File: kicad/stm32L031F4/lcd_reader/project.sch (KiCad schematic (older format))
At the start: 32 parts, among them J1 WAKE, J10 TEST_1P, J11 TEST_1P, J12 TEST_1P, J2 SWD, J3 TEST_1P, J4 TEST_1P, J5 TEST_1P, J6 LCD, J7 TEST_1P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

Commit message: Labels
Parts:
- added J13: GND_EXT, Pin_Headers:Pin_Header_Straight_1x01_Pitch2.54mm, symbol CONN_01X01
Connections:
- net GND: now also J13.1 (P1)
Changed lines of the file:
@@
 Wire Wire Line
 	3375 4900 3975 4900
+$Comp
+L CONN_01X01 J13
+U 1 1 5A01BD9F
+P 9900 5500
+F 0 "J13" H 9900 5600 50  0000 C CNN
+F 1 "GND_EXT" V 10000 5500 50  0000 C CNN
+F 2 "Pin_Headers:Pin_Header_Straight_1x01_Pitch2.54mm" H 9900 5500 50  0001 C CNN
+F 3 "" H 9900 5500 50  0001 C CNN
+	1    9900 5500
+	1    0    0    -1
+$EndComp
 $EndSCHEMATC

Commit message: Silkscreen tidying
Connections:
- net COM1: now also J6.1 (P1); no longer J6.9 (P9)
- net at R10.2, U3.13: now also J6.9 (P9); no longer J6.1 (P1)
- net at R9.2, U3.11: now also J6.8 (P8); no longer J6.2 (P2)
- net at R8.2, U3.9: now also J6.7 (P7); no longer J6.3 (P3)
- net at R7.2, U3.5: now also J6.6 (P6); no longer J6.4 (P4)
- net at R5.2, U1.11: now also J6.4 (P4); no longer J6.6 (P6)
- net at R4.2, U1.9: now also J6.3 (P3); no longer J6.7 (P7)
- net at R3.2, U1.5: now also J6.2 (P2); no longer J6.8 (P8)
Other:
- moved on the sheet: C4, C5, J10, J11, J12, J3, J4, J5, J6, J7, J9, R10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

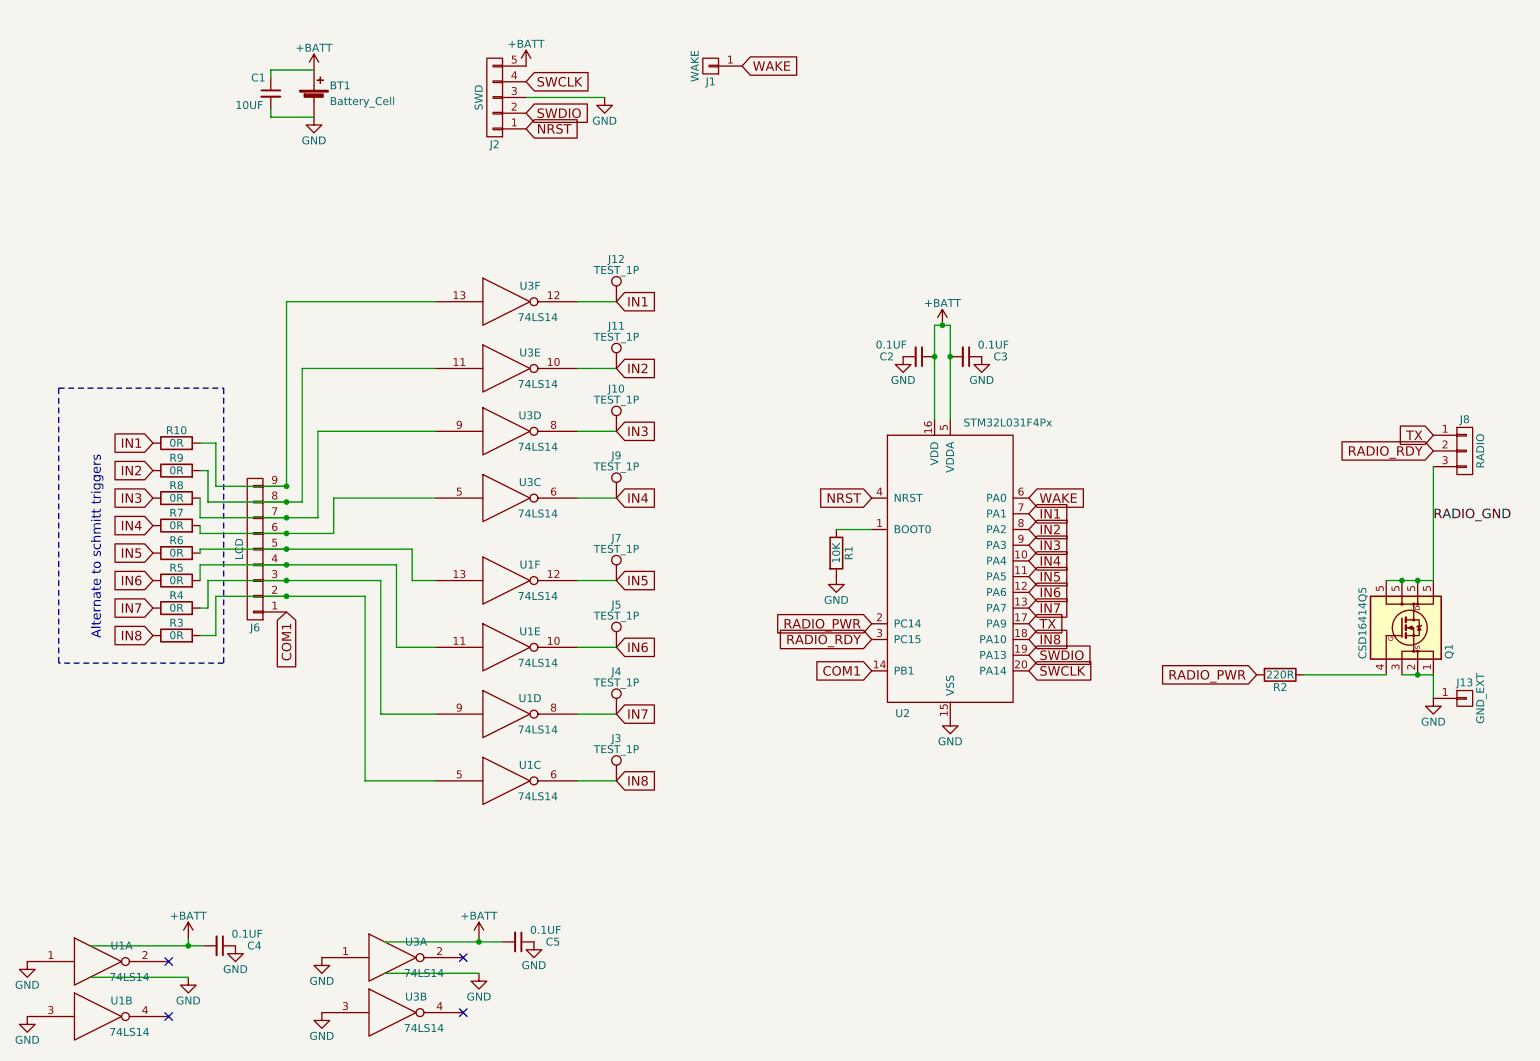
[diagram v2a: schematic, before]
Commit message: Start of zebra strip compatability
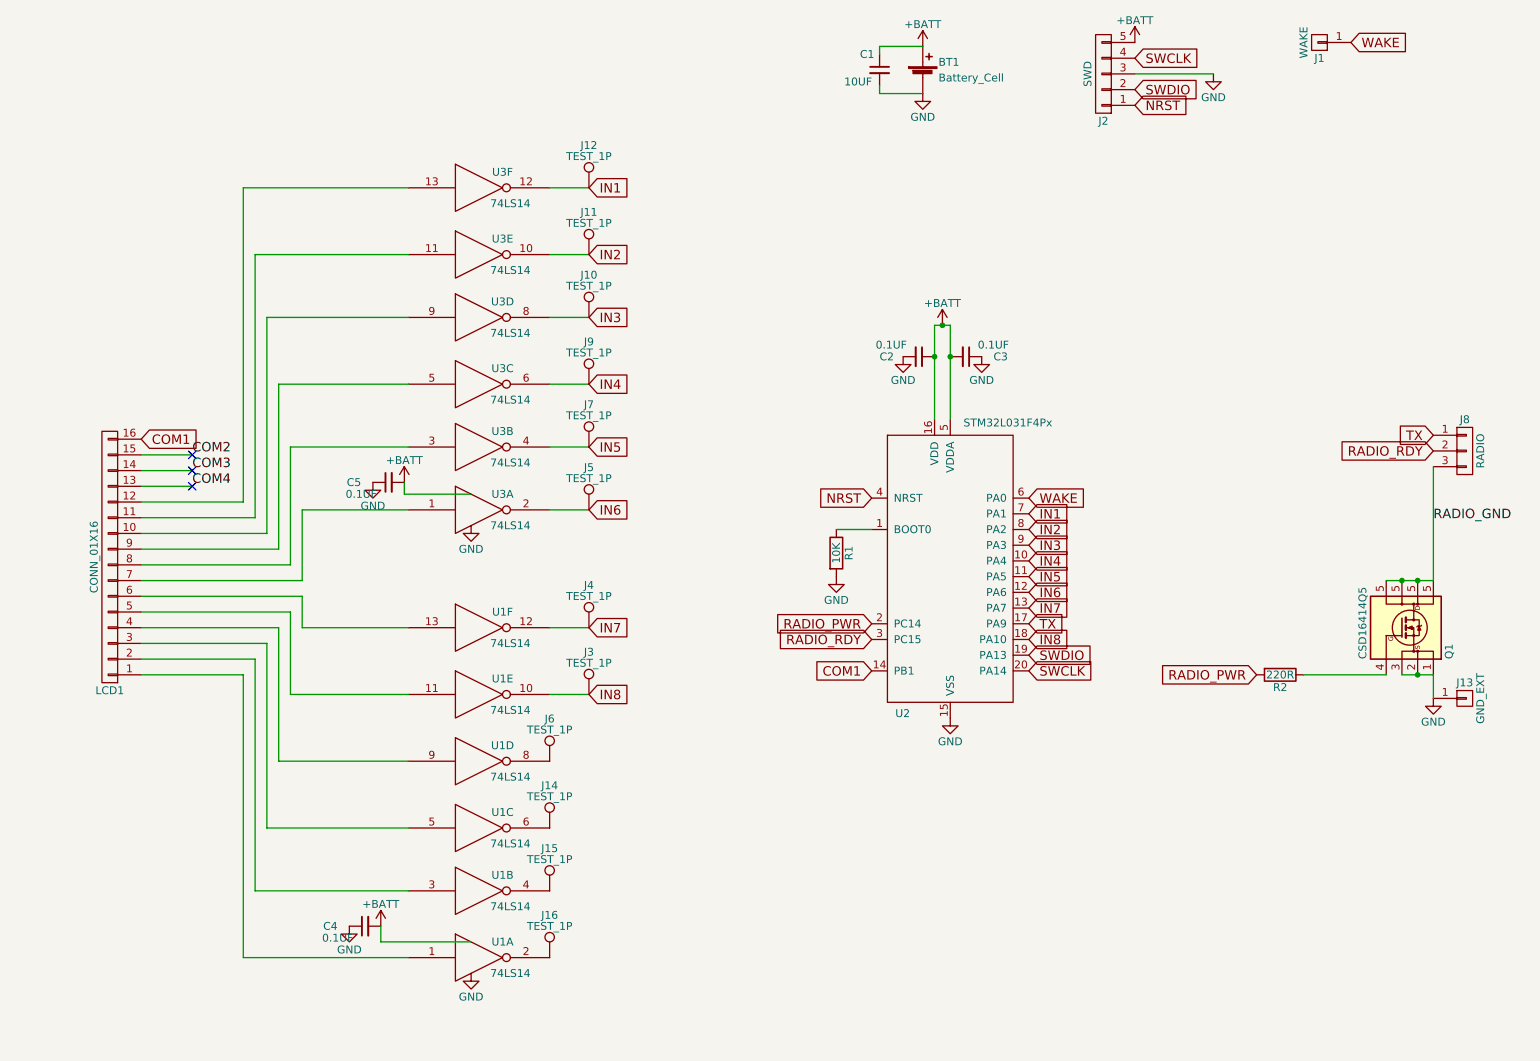
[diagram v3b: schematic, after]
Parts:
- removed J6: LCD, Pin_Headers:Pin_Header_Straight_1x09_Pitch2.54mm, symbol CONN_01X09
- removed R10, R3, R4, R5, R6, R7, R8, R9: 0R, Resistors_SMD:R_0603_HandSoldering, symbol R
- added J14, J15, J16, J6: TEST_1P, Connectors_TestPoints:Test_Point_Pad_d1.0mm, symbol TEST_1P
- added LCD1: CONN_01X16, theapi:ZEBRA-16, symbol CONN_01X16
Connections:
- net COM1: now also LCD1.16 (P16)
- net GND: no longer U1.1, U1.3, U3.1, U3.3
- net IN5: now also U3.4; no longer U1.12
- net IN6: now also U3.2; no longer U1.10
- net IN7: now also U1.12; no longer U1.8
- net IN8: now also U1.10; no longer U1.6
- net at U3.13: now also LCD1.12 (P12)
- net at U3.11: now also LCD1.11 (P11)
- net at U1.5: now also LCD1.3 (P3)
- net at U1.9: now also LCD1.4 (P4)
- net at U1.11: now also LCD1.5 (P5)
- net at U1.13: now also LCD1.6 (P6)
- net at U3.5: now also LCD1.9 (P9)
- net at U3.9: now also LCD1.10 (P10)
- net at U1.4: now also J15.1
- net at U1.2: now also J16.1
- new net: J6.1, U1.8
- new net: J14.1, U1.6
- new net: LCD1.8 (P8), U3.3
- new net: LCD1.7 (P7), U3.1
- new net: LCD1.2 (P2), U1.3
- new net: LCD1.1 (P1), U1.1
- new net COM2: LCD1.15 (P15)
- new net COM3: LCD1.14 (P14)
- new net COM4: LCD1.13 (P13)
- no-connect marks 4 -> 3
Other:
- note removed: "Alternate to schmitt triggers"
- moved on the sheet: BT1, C1, C4, C5, J1, J10, J11, J12, J2, J3, J4, J5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

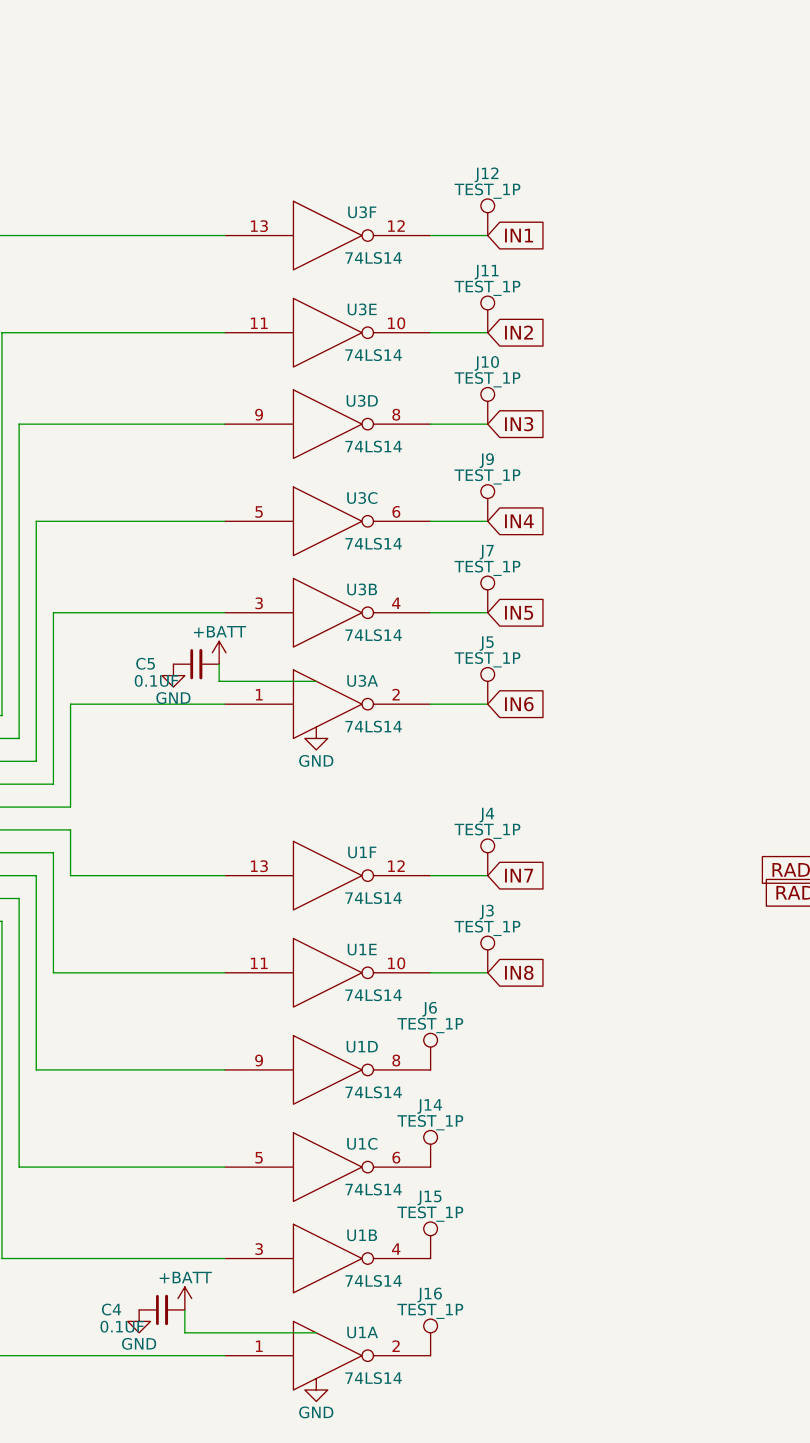
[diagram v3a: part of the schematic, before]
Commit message: Layout for sandwiched zebra connector
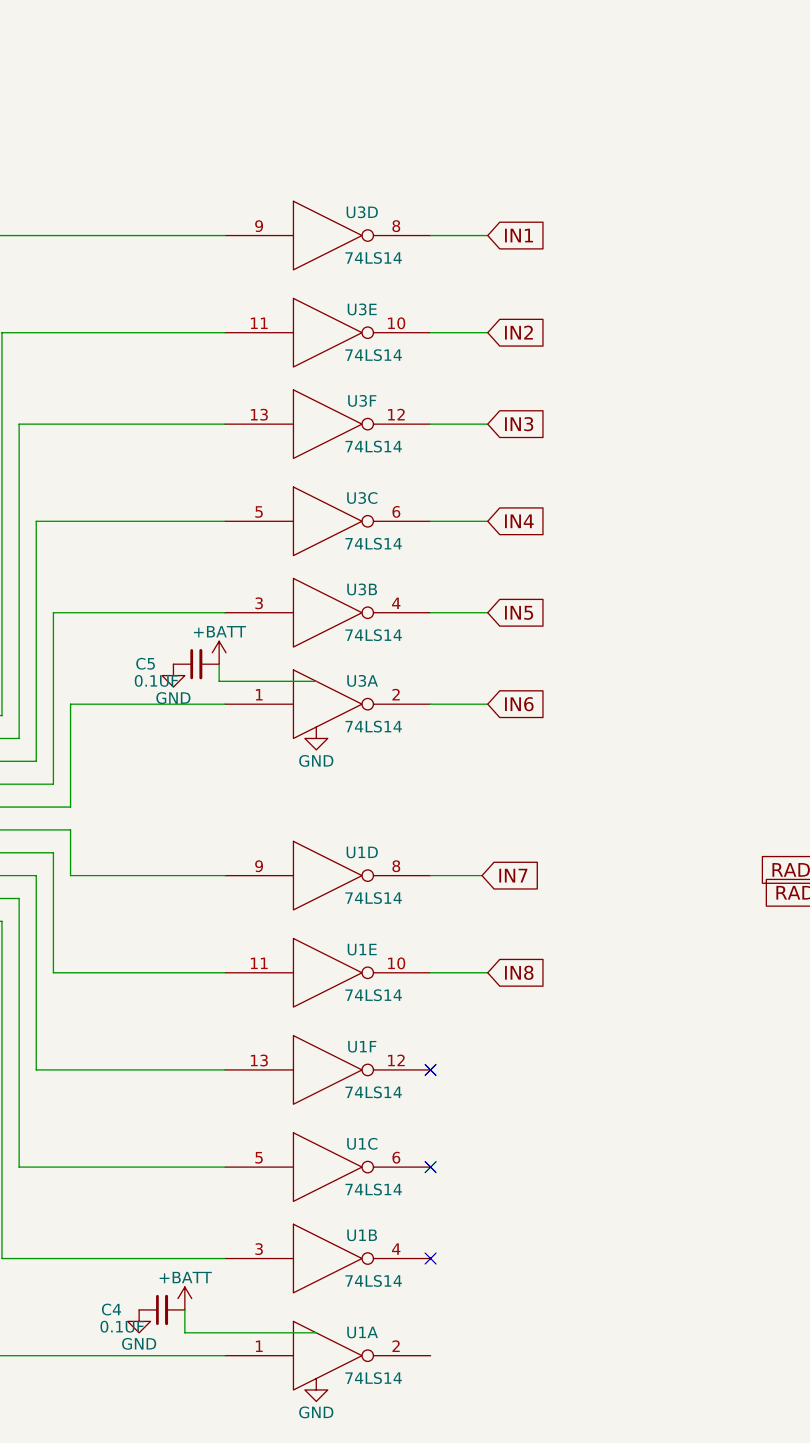
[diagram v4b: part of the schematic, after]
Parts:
- removed J10, J11, J12, J14, J15, J16, J3, J4, J5, J6, J7, J9: TEST_1P, Connectors_TestPoints:Test_Point_Pad_d1.0mm, symbol TEST_1P
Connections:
- net IN1: now also U3.8; no longer U3.12
- net IN3: now also U3.12; no longer U3.8
- net IN7: now also U1.8; no longer U1.12
- net at U3.13: now also LCD1.10 (P10); no longer LCD1.12 (P12)
- net at U3.9: now also LCD1.12 (P12); no longer LCD1.10 (P10)
- net at U1.13: now also LCD1.4 (P4); no longer LCD1.6 (P6)
- net at U1.9: now also LCD1.6 (P6); no longer LCD1.4 (P4)
- no-connect marks 3 -> 6
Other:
- moved on the sheet: U1D, U1F, U3D, U3F
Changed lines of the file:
@@
 Text GLabel 4325 4300 2    60   Input ~ 0
 IN6
-Text GLabel 4325 5050 2    60   Input ~ 0
+Text GLabel 4300 5050 2    60   Input ~ 0
 IN7
 Text GLabel 4325 5475 2    60   Input ~ 0
@@
 L 74LS14 U3
 U 6 1 5A009C2E
-P 3625 2250
-F 0 "U3" H 3775 2350 50  0000 C CNN
-F 1 "74LS14" H 3825 2150 50  0000 C CNN
-F 2 "SMD_Packages:SSOP-14" H 3625 2250 50  0001 C CNN
-F 3 "" H 3625 2250 50  0001 C CNN
-	6    3625 2250
+P 3625 3075
+F 0 "U3" H 3775 3175 50  0000 C CNN
+F 1 "74LS14" H 3825 2975 50  0000 C CNN
+F 2 "SMD_Packages:SSOP-14" H 3625 3075 50  0001 C CNN
+F 3 "" H 3625 3075 50  0001 C CNN
+	6    3625 3075
 	1    0    0    -1
 $EndComp
@@
 L 74LS14 U3
 U 4 1 5A00A171
-P 3625 3075
-F 0 "U3" H 3775 3175 50  0000 C CNN
-F 1 "74LS14" H 3825 2975 50  0000 C CNN
-F 2 "SMD_Packages:SSOP-14" H 3625 3075 50  0001 C CNN
-F 3 "" H 3625 3075 50  0001 C CNN
-	4    3625 3075
+P 3625 2250
+F 0 "U3" H 3775 2350 50  0000 C CNN
+F 1 "74LS14" H 3825 2150 50  0000 C CNN
+F 2 "SMD_Packages:SSOP-14" H 3625 2250 50  0001 C CNN
+F 3 "" H 3625 2250 50  0001 C CNN
+	4    3625 2250
 	1    0    0    -1
 $EndComp
@@
 L 74LS14 U1
 U 6 1 5A00A342
-P 3625 5050
-F 0 "U1" H 3775 5150 50  0000 C CNN
-F 1 "74LS14" H 3825 4950 50  0000 C CNN
-F 2 "SMD_Packages:SSOP-14" H 3625 5050 50  0001 C CNN
-F 3 "" H 3625 5050 50  0001 C CNN
-	6    3625 5050
+P 3625 5900
+F 0 "U1" H 3775 6000 50  0000 C CNN
+F 1 "74LS14" H 3825 5800 50  0000 C CNN
+F 2 "SMD_Packages:SSOP-14" H 3625 5900 50  0001 C CNN
+F 3 "" H 3625 5900 50  0001 C CNN
+	6    3625 5900
 	1    0    0    -1
 $EndComp
@@
 L 74LS14 U1
 U 4 1 5A00A47D
-P 3625 5900
-F 0 "U1" H 3775 6000 50  0000 C CNN
-F 1 "74LS14" H 3825 5800 50  0000 C CNN
-F 2 "SMD_Packages:SSOP-14" H 3625 5900 50  0001 C CNN
-F 3 "" H 3625 5900 50  0001 C CNN
-	4    3625 5900
+P 3625 5050
+F 0 "U1" H 3775 5150 50  0000 C CNN
+F 1 "74LS14" H 3825 4950 50  0000 C CNN
+F 2 "SMD_Packages:SSOP-14" H 3625 5050 50  0001 C CNN
+F 3 "" H 3625 5050 50  0001 C CNN
+	4    3625 5050
 	1    0    0    -1
 $EndComp
@@
 F 3 "" H 3625 7150 50  0001 C CNN
 	1    3625 7150
-	1    0    0    -1
-$EndComp
-$Comp
-L TEST_1P J3
-U 1 1 5A00C3BD
-P 4325 5475
-F 0 "J3" H 4325 5745 50  0000 C CNN
-F 1 "TEST_1P" H 4325 5675 50  0000 C CNN
-F 2 "Connectors_TestPoints:Test_Point_Pad_d1.0mm" H 4525 5475 50  0001 C CNN
-F 3 "" H 4525 5475 50  0001 C CNN
-	1    4325 5475
-	1    0    0    -1
-$EndComp
-$Comp
-L TEST_1P J4
-U 1 1 5A00C5C2
-P 4325 5050
-F 0 "J4" H 4325 5320 50  0000 C CNN
-F 1 "TEST_1P" H 4325 5250 50  0000 C CNN
-F 2 "Connectors_TestPoints:Test_Point_Pad_d1.0mm" H 4525 5050 50  0001 C CNN
-F 3 "" H 4525 5050 50  0001 C CNN
-	1    4325 5050
-	1    0    0    -1
-$EndComp
-$Comp
-L TEST_1P J5
-U 1 1 5A00C62C
-P 4325 4300
-F 0 "J5" H 4325 4570 50  0000 C CNN
-F 1 "TEST_1P" H 4325 4500 50  0000 C CNN
-F 2 "Connectors_TestPoints:Test_Point_Pad_d1.0mm" H 4525 4300 50  0001 C CNN
-F 3 "" H 4525 4300 50  0001 C CNN
-	1    4325 4300
-	1    0    0    -1
-$EndComp
-$Comp
-L TEST_1P J7
-U 1 1 5A00C69B
-P 4325 3900
-F 0 "J7" H 4325 4170 50  0000 C CNN
-F 1 "TEST_1P" H 4325 4100 50  0000 C CNN
-F 2 "Connectors_TestPoints:Test_Point_Pad_d1.0mm" H 4525 3900 50  0001 C CNN
-F 3 "" H 4525 3900 50  0001 C CNN
-	1    4325 3900
-	1    0    0    -1
-$EndComp
-$Comp
-L TEST_1P J9
-U 1 1 5A00CA23
-P 4325 3500
-F 0 "J9" H 4325 3770 50  0000 C CNN
-F 1 "TEST_1P" H 4325 3700 50  0000 C CNN
-F 2 "Connectors_TestPoints:Test_Point_Pad_d1.0mm" H 4525 3500 50  0001 C CNN
-F 3 "" H 4525 3500 50  0001 C CNN
-	1    4325 3500
-	1    0    0    -1
-$EndComp
-$Comp
-L TEST_1P J10
-U 1 1 5A00CAF9
-P 4325 3075
-F 0 "J10" H 4325 3345 50  0000 C CNN
-F 1 "TEST_1P" H 4325 3275 50  0000 C CNN
-F 2 "Connectors_TestPoints:Test_Point_Pad_d1.0mm" H 4525 3075 50  0001 C CNN
-F 3 "" H 4525 3075 50  0001 C CNN
-	1    4325 3075
-	1    0    0    -1
-$EndComp
-$Comp
-L TEST_1P J11
-U 1 1 5A00CBC6
-P 4325 2675
-F 0 "J11" H 4325 2945 50  0000 C CNN
-F 1 "TEST_1P" H 4325 2875 50  0000 C CNN
-F 2 "Connectors_TestPoints:Test_Point_Pad_d1.0mm" H 4525 2675 50  0001 C CNN
-F 3 "" H 4525 2675 50  0001 C CNN
-	1    4325 2675
-	1    0    0    -1
-$EndComp
-$Comp
-L TEST_1P J12
-U 1 1 5A00CC3C
-P 4325 2250
-F 0 "J12" H 4325 2520 50  0000 C CNN
-F 1 "TEST_1P" H 4325 2450 50  0000 C CNN
-F 2 "Connectors_TestPoints:Test_Point_Pad_d1.0mm" H 4525 2250 50  0001 C CNN
-F 3 "" H 4525 2250 50  0001 C CNN
-	1    4325 2250
 	1    0    0    -1
 $EndComp
@@
 	9700 4750 9700 4025
 Wire Wire Line
+	4075 3075 4325 3075
+Wire Wire Line
+	4075 2675 4325 2675
+Wire Wire Line
 	4075 2250 4325 2250
 Wire Wire Line
-	4075 2675 4325 2675
-Wire Wire Line
-	4075 3075 4325 3075
-Wire Wire Line
 	4075 3500 4325 3500
 Wire Wire Line
@@
 Wire Wire Line
 	4075 4300 4325 4300
-Wire Wire Line
-	4075 5050 4325 5050
 Wire Wire Line
 	4075 5475 4325 5475
@@
 Wire Wire Line
 	3150 4200 3575 4200
-$Comp
-L TEST_1P J6
-U 1 1 5A035323
-P 4075 5900
-F 0 "J6" H 4075 6170 50  0000 C CNN
-F 1 "TEST_1P" H 4075 6100 50  0000 C CNN
-F 2 "Connectors_TestPoints:Test_Point_Pad_d1.0mm" H 4275 5900 50  0001 C CNN
-F 3 "" H 4275 5900 50  0001 C CNN
-	1    4075 5900
-	1    0    0    -1
-$EndComp
 Wire Wire Line
 	3000 7050 3000 6950
@@
 Wire Wire Line
 	3150 4200 3150 4125
-$Comp
-L TEST_1P J14
-U 1 1 5A03681F
-P 4075 6325
-F 0 "J14" H 4075 6595 50  0000 C CNN
-F 1 "TEST_1P" H 4075 6525 50  0000 C CNN
-F 2 "Connectors_TestPoints:Test_Point_Pad_d1.0mm" H 4275 6325 50  0001 C CNN
-F 3 "" H 4275 6325 50  0001 C CNN
-	1    4075 6325
-	1    0    0    -1
-$EndComp
-$Comp
-L TEST_1P J15
-U 1 1 5A0368AF
-P 4075 6725
-F 0 "J15" H 4075 6995 50  0000 C CNN
-F 1 "TEST_1P" H 4075 6925 50  0000 C CNN
-F 2 "Connectors_TestPoints:Test_Point_Pad_d1.0mm" H 4275 6725 50  0001 C CNN
-F 3 "" H 4275 6725 50  0001 C CNN
-	1    4075 6725
-	1    0    0    -1
-$EndComp
-$Comp
-L TEST_1P J16
-U 1 1 5A03693A
-P 4075 7150
-F 0 "J16" H 4075 7420 50  0000 C CNN
-F 1 "TEST_1P" H 4075 7350 50  0000 C CNN
-F 2 "Connectors_TestPoints:Test_Point_Pad_d1.0mm" H 4275 7150 50  0001 C CNN
-F 3 "" H 4275 7150 50  0001 C CNN
-	1    4075 7150
-	1    0    0    -1
-$EndComp
+Wire Wire Line
+	4075 5050 4300 5050
+NoConn ~ 4075 5900
+NoConn ~ 4075 6325
+NoConn ~ 4075 6725
 $EndSCHEMATC
